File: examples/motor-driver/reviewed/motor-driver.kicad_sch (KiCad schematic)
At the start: 17 parts, among them J1 VM 2.7-10.8V, J2 MOTOR A, J3 MOTOR B, J4 LOGIC, U1 DRV8833PW

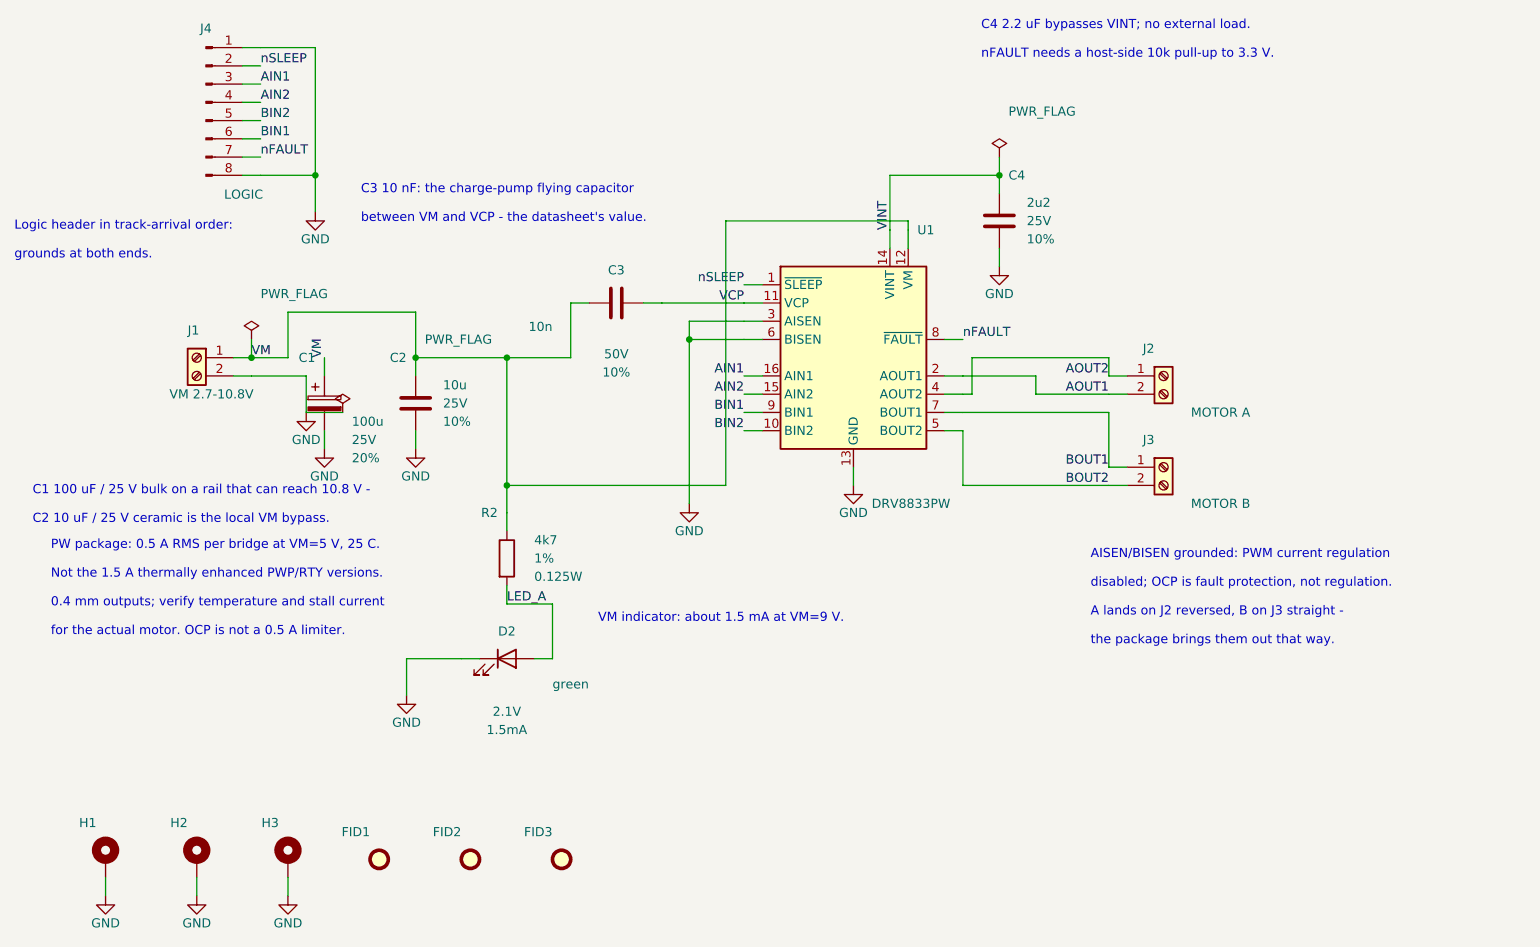
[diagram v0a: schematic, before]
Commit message: chore(examples): regenerate the four two-layer boards and their pictures
buck-5v, motor-driver, pico-carrier and opamp-filter, regenerated from the
merged generator and gated clean on KiCad 9.0.9. The inner-layer pictures go
with the inner layers.

fpga-audio is still routing; it follows.

Co-Authored-By: Claude Opus 5 <noreply@anthropic.com>
Claude-Session: https://claude.ai/code/session_01XQE7UkE9WTSMW3oZ3kLeCt
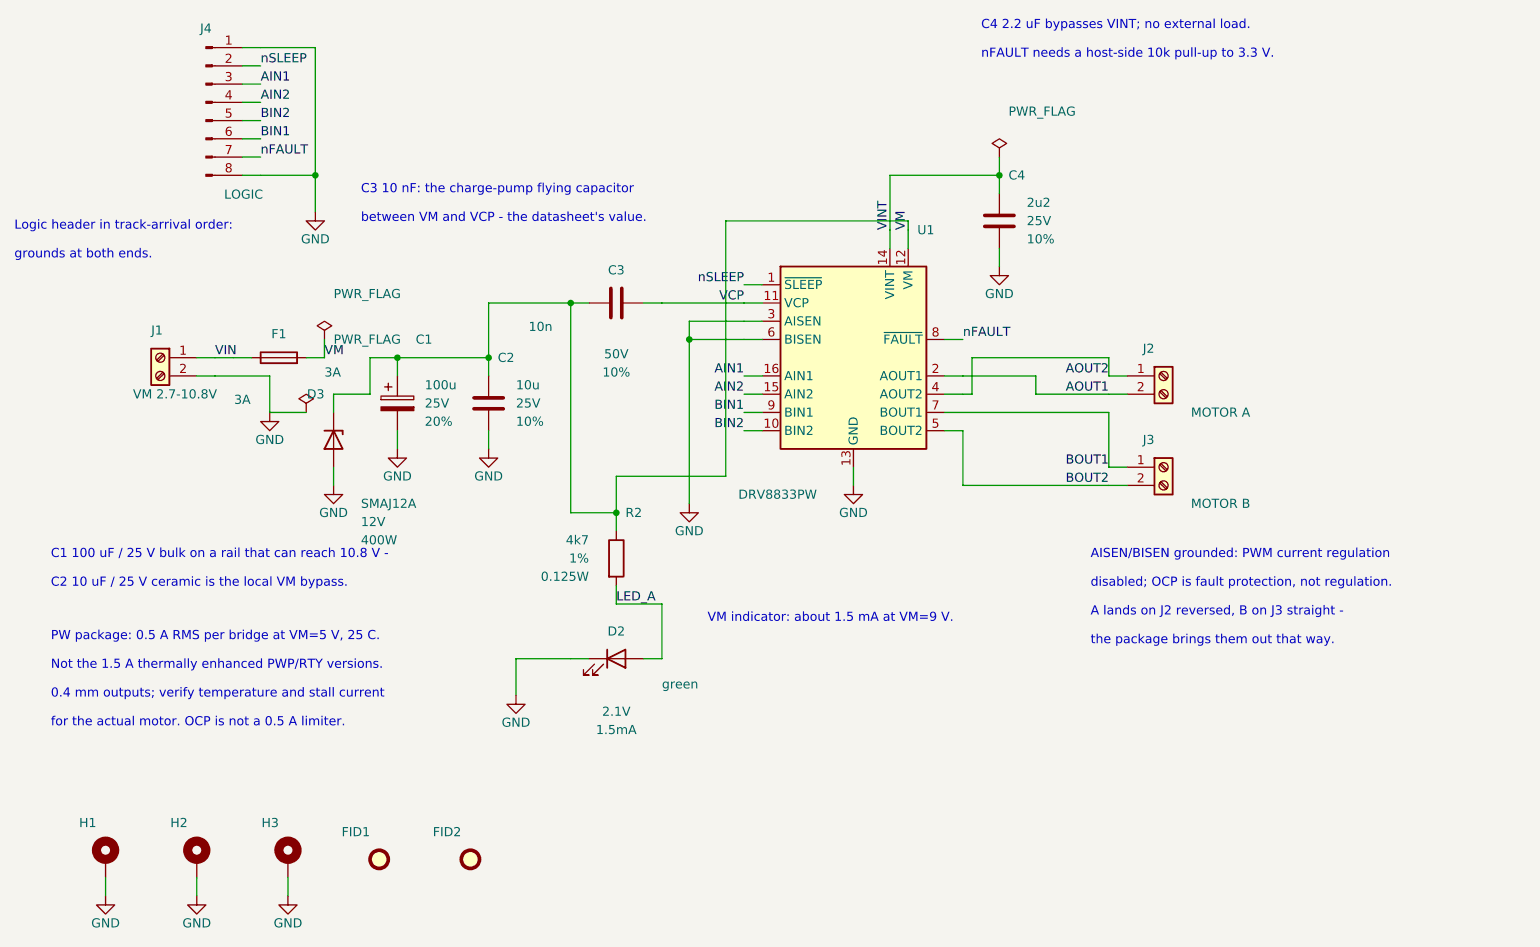
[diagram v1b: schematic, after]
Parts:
- removed FID3: Fiducial, Fiducial:Fiducial_1mm_Mask2mm, symbol Mechanical:Fiducial
- added D3: SMAJ12A, Diode_SMD:D_SMA, symbol Device:D_Zener
- added F1: 3A, Fuse:Fuse_1206_3216Metric, symbol Device:Fuse
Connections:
- net GND: now also D3.2 (A)
- net VM: now also D3.1 (K), F1.2; no longer J1.1 (Pin_1)
- new net VIN: F1.1, J1.1 (Pin_1)
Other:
- moved on the sheet: C1, C2, D2, J1, R2

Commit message: feat(examples): route the nets with something to lose first, and never behind a plain one
The reviewer circled a column of ten vias on the motor driver: the four
0.4 mm bridge outputs and nFAULT each hopped under one 0.3 mm logic input
that had toured the west end of the board and been promoted to the front
for it. Two causes: the search charged the plane surcharge on a link the
design had declared on the back, and the header pin sat on the far side of
AIN2's stated lane from its via.

The routing order now has two classes. A link wider than the board's
thinnest, or on a net the design names in priority_nets, is routed while
the board is empty; a rip-up or a detour chase promotes a plain link only
to the front of the plain links, so it goes round. A plain link with no
lane even there is lifted ahead of the priority nets and the log says so:
a floorplan with no room, the placement's problem. A link declared on the
back and kept there pays the router's ordinary rate. resolve_routes and
the two helpers join the route-cache key, as does priority_nets.

Per board: motor-driver's J4 pins reordered to the order the drops land,
and AIN2's lane turns where its last leg is a 45; the bridge outputs and
nFAULT now route straight with zero vias, on the first pass. opamp-filter
names its filter path and fences its three connectors; fpga-audio names
its rails (distributed at signal width by design), the clock and the I2S
bus. All five cold-route clean: gates, contracts and KiCad DRC pass.

Also fix the loop cutter: it split a back-side run at a front-side pad it
passed under, manufactured a node the front stub shared, read a cycle and
cut the stub and its via. The split now respects the pad's layer, with a
test that shows the old cutter losing the via.

Co-Authored-By: Claude Fable 5.1 <noreply@anthropic.com>
Claude-Session: https://claude.ai/code/session_01XQE7UkE9WTSMW3oZ3kLeCt
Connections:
- net AIN1: now also J4.5 (Pin_5); no longer J4.3 (Pin_3)
- net AIN2: now also J4.3 (Pin_3); no longer J4.4 (Pin_4)
- net BIN1: now also J4.4 (Pin_4); no longer J4.6 (Pin_6)
- net BIN2: now also J4.6 (Pin_6); no longer J4.5 (Pin_5)
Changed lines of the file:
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@@
   (label "nSLEEP" (at 46.99 39.37 0) (effects (font (size 1.27 1.27)) (justify left bottom)))
   (wire (pts (xy 44.45 41.91) (xy 46.99 41.91)) (stroke (width 0) (type default)))
-  (label "AIN1" (at 46.99 41.91 0) (effects (font (size 1.27 1.27)) (justify left bottom)))
+  (label "AIN2" (at 46.99 41.91 0) (effects (font (size 1.27 1.27)) (justify left bottom)))
   (wire (pts (xy 44.45 44.45) (xy 46.99 44.45)) (stroke (width 0) (type default)))
-  (label "AIN2" (at 46.99 44.45 0) (effects (font (size 1.27 1.27)) (justify left bottom)))
+  (label "BIN1" (at 46.99 44.45 0) (effects (font (size 1.27 1.27)) (justify left bottom)))
   (wire (pts (xy 44.45 46.99) (xy 46.99 46.99)) (stroke (width 0) (type default)))
-  (label "BIN2" (at 46.99 46.99 0) (effects (font (size 1.27 1.27)) (justify left bottom)))
+  (label "AIN1" (at 46.99 46.99 0) (effects (font (size 1.27 1.27)) (justify left bottom)))
   (wire (pts (xy 44.45 49.53) (xy 46.99 49.53)) (stroke (width 0) (type default)))
-  (label "BIN1" (at 46.99 49.53 0) (effects (font (size 1.27 1.27)) (justify left bottom)))
+  (label "BIN2" (at 46.99 49.53 0) (effects (font (size 1.27 1.27)) (justify left bottom)))
   (wire (pts (xy 44.45 52.07) (xy 46.99 52.07)) (stroke (width 0) (type default)))
   (label "nFAULT" (at 46.99 52.07 0) (effects (font (size 1.27 1.27)) (justify left bottom)))
